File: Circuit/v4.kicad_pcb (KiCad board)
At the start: 2 copper layers, 30 x 50 mm, 43 parts, among them J2 AVR-ISP-6, Q1 IRLML6244TRPBF, U1 HMHA2801, U4 ATtiny841-SSU

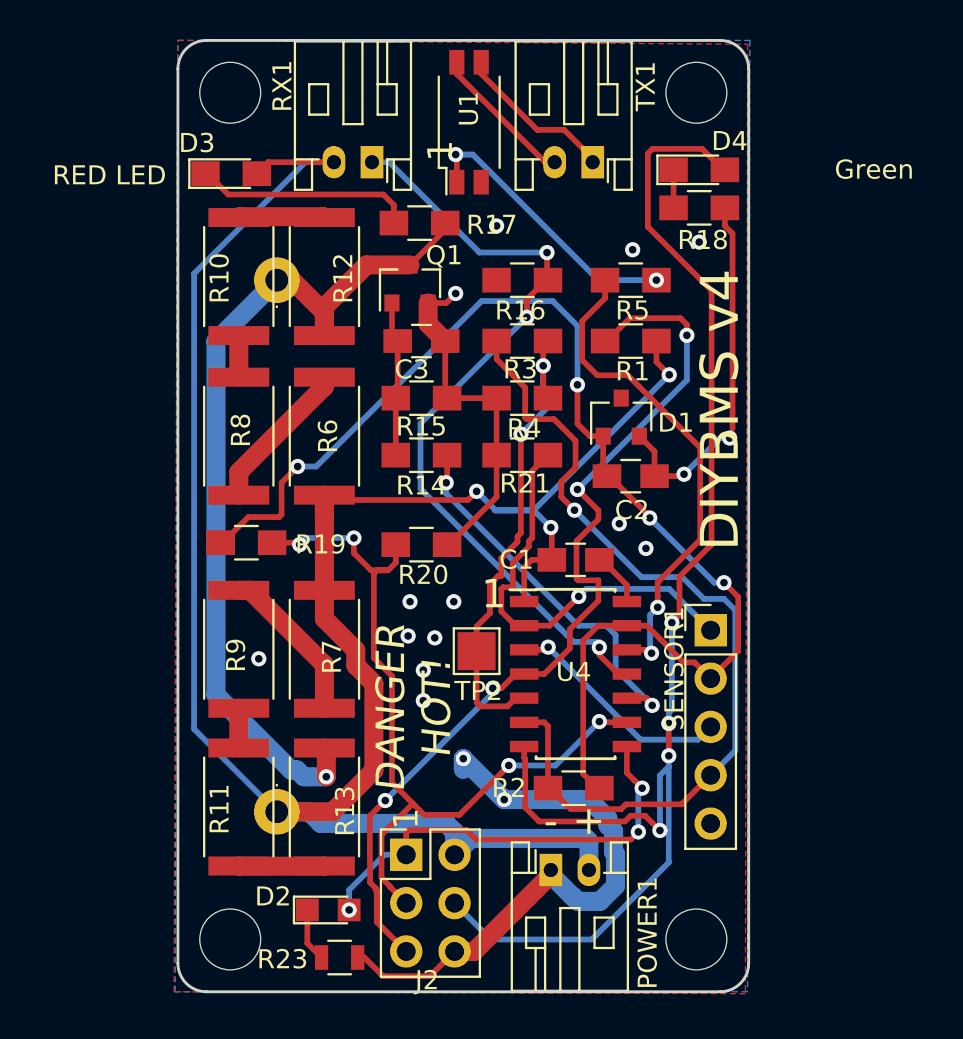
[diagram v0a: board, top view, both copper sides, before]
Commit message: add jlcpcb_assembly branch
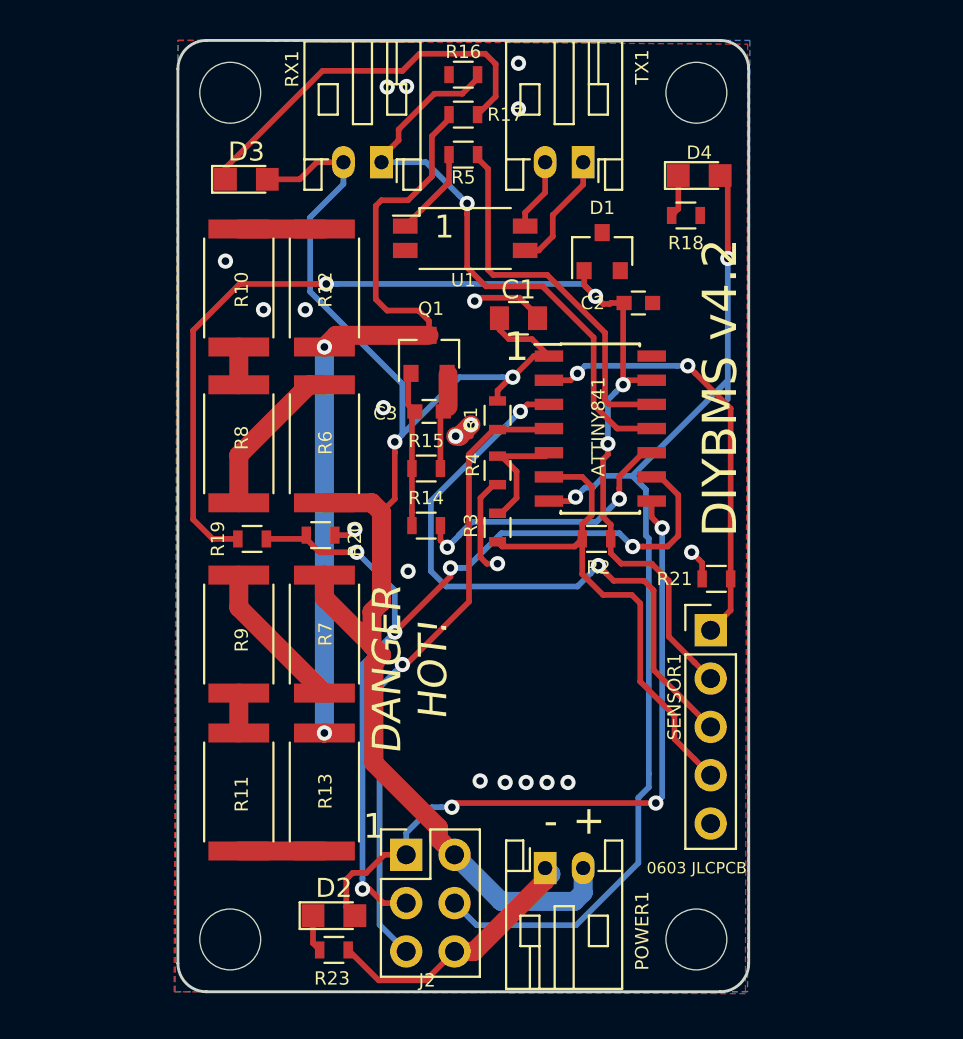
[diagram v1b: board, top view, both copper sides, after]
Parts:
- removed R22: 4R4, Resistors_THT:R_Axial_Power_L25.0mm_W9.0mm_P27.94mm
- removed TP2: TestPoint, TestPoint:TestPoint_Pad_2.0x2.0mm
- removed U4: ATtiny841-SSU, Housings_SOIC:SOIC-14_3.9x8.7mm_Pitch1.27mm
- added ATTINY841: ATtiny841-SSU, Housings_SOIC:SOIC-14_3.9x8.7mm_Pitch1.27mm, F.Cu at (124.1, 68.4)
- C1: footprint Capacitors_SMD:C_0805_HandSoldering -> Capacitors_SMD:C_0805
- C2: footprint Capacitors_SMD:C_0805_HandSoldering -> Capacitors_SMD:C_0603
- C3: value 10uF 10V -> MLCC 10UF 10V; footprint Capacitors_SMD:C_0805_HandSoldering -> Capacitors_SMD:C_0603
- D1: value LM4040BIM3-2.0/NOPB, 2.048V, SOT-23-3 -> ADR5040BRTZ-REEL7 2.048V
- D3: value RED LED -> Red; footprint LEDs:LED_0805_HandSoldering -> LEDs:LED_0805
- D4: footprint LEDs:LED_0805_HandSoldering -> LEDs:LED_0805
- R1, R14, R15, R16, R17, R18, R2, R20, R21, R5: footprint Resistors_SMD:R_0805_HandSoldering -> Resistors_SMD:R_0603
- R10, R11, R12, R13, R6, R7, R8, R9: value 2R2 1W -> 2R 1W
- R19: value SDNT2012X473F4150FTF -> NCP18WB473J03RB; footprint Resistors_SMD:R_0805_HandSoldering -> Resistors_SMD:R_0603
- R23: value 2K2 -> 1K8; footprint Resistors_SMD:R_0805 -> Resistors_SMD:R_0603
- R3: value 475K E96 series (tolerance 1%) -> 470KOHMS ±1% 1/10W; footprint Resistors_SMD:R_0805_HandSoldering -> Resistors_SMD:R_0603
- R4: value 402K E96 series (tolerance 1%) -> 390KOHMS ±1% 1/10W; footprint Resistors_SMD:R_0805_HandSoldering -> Resistors_SMD:R_0603
- U1: value HMHA2801 -> EL3H7(B)(TA)-G
- moved R2 13.2 mm to (123.9, 74.2)
- moved C1 13.0 mm to (119.8, 62.6)
- moved R21 12.1 mm to (130.2, 76.3)
- moved R16 11.2 mm to (116.9, 49.8)
- moved R5 11.0 mm to (116.9, 54.0), turned to 0 degrees
- moved R3 9.89 mm to (118.7, 73.6), turned to 90 degrees
- moved C2 9.11 mm to (126.1, 61.8)
- moved D1 8.76 mm to (124.2, 59.1)
- moved R1 8.01 mm to (118.7, 67.7), turned to 270 degrees
- moved R17 6.15 mm to (116.9, 51.9), turned to 0 degrees
- moved U1 6.10 mm to (117.0, 58.4), turned to 0 degrees
- moved R20 5.32 mm to (109.4, 74.0)
- moved R4 4.02 mm to (118.7, 70.6), turned to 270 degrees
- moved Q1 3.83 mm to (115.1, 64.5)
- moved C3 3.72 mm to (115.1, 67.5)
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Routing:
- net VCC: track 118.8 -> 80.1 mm, vias 3 -> 2
- net GND: track 71.1 -> 33.4 mm, vias 17 -> 20
- net Net-(ATTINY841-Pad3): track 12.2 -> 33.4 mm, vias 1 -> 2
- net ENABLE: track 46.2 -> 26.2 mm, vias 1 -> 0
- net Net-(ATTINY841-Pad5): track 25.4 -> 6.84 mm, vias 2 -> 0
- net Net-(ATTINY841-Pad7): track 72.5 -> 56.6 mm, vias 4 -> 2
- net Net-(ATTINY841-Pad4): track 49.2 -> 33.5 mm, vias 4 -> 1
- net Net-(ATTINY841-Pad8): track 23.5 -> 36.9 mm
- net RXD0: track 41.7 -> 31.6 mm, vias 3 -> 1
- net Net-(R5-Pad1): track 14.8 -> 4.71 mm, vias 2 -> 0
- net Net-(D3-Pad1): track 11.5 -> 20.6 mm
- net Net-(ATTINY841-Pad9): track 42.6 -> 48.9 mm, vias 4 -> 5
- net TXD0: track 26.1 -> 19.9 mm, vias 2 -> 0
- net DUMP_LOAD_ENABLE: track 20.1 -> 14.8 mm
- net Net-(Q1-Pad3): track 46.6 -> 42.2 mm, vias 1 -> 2
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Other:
- board text added: "0603 JLCPCB"
- board text added: "1 Jan 2020"
- board text added: "DIYBMS v4.2"
- board text added: "©2019/2020 Stuart Pittaway"
- board text removed: "23 June 2019"
- board text removed: "DIYBMS v4"
- board text removed: "©2019 Stuart Pittaway"

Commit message: Updated BOM and CPL files
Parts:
- C3: value MLCC 10UF 10V -> 10uF X5R
- Q1: value IRLML6244TRPBF -> AO3400A
- R1: value 10K -> 10KOHMS
- R10, R11, R12, R13, R6, R7, R8, R9: value 2R 1W -> 2OHMS
- R14, R5: value 510R -> 510OHMS
- R15, R20, R21: value 47K -> 47KOHMS
- R16: value 4K7 -> 4.7KOHMS
- R17, R18: value 2K2 -> 2.2KOHMS
- R2: value 1K -> 1KOHMS
- R23: value 1K8 -> 1.8KOHMS
- R3: value 470KOHMS ±1% 1/10W -> 470KOHMS
- R4: value 390KOHMS ±1% 1/10W -> 390KOHMS
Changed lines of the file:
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@@
   (page A4)
   (layers
-    (0 F.Cu signal hide)
-    (31 B.Cu signal hide)
+    (0 F.Cu signal)
+    (31 B.Cu signal)
     (32 B.Adhes user)
     (33 F.Adhes user hide)
@@
       (effects (font (size 0.7 0.7) (thickness 0.1)))
     )
-    (fp_text value 1K8 (at -1.3 -1 180) (layer F.Fab) hide
+    (fp_text value 1.8KOHMS (at -1.3 -1 180) (layer F.Fab) hide
       (effects (font (size 0.7 0.7) (thickness 0.1)))
     )
@@
       (effects (font (size 0.7 0.7) (thickness 0.1)))
     )
-    (fp_text value 47K (at -0.5 1.2 180) (layer F.Fab)
+    (fp_text value 47KOHMS (at -0.5 1.2 180) (layer F.Fab)
       (effects (font (size 0.7 0.7) (thickness 0.1)))
     )
@@
       (effects (font (size 0.7 0.7) (thickness 0.1)))
     )
-    (fp_text value 47K (at 0 1.5) (layer F.Fab)
+    (fp_text value 47KOHMS (at 0 1.5) (layer F.Fab)
       (effects (font (size 0.7 0.7) (thickness 0.1)))
     )
@@
       (effects (font (size 0.7 0.7) (thickness 0.1)))
     )
-    (fp_text value 2K2 (at -0.8 -2.7 180) (layer F.Fab)
+    (fp_text value 2.2KOHMS (at -0.8 -2.7 180) (layer F.Fab)
       (effects (font (size 0.7 0.7) (thickness 0.1)))
     )
@@
       (effects (font (size 0.7 0.7) (thickness 0.1)))
     )
-    (fp_text value 2K2 (at 0 -0.1) (layer F.Fab)
+    (fp_text value 2.2KOHMS (at 0 -0.1) (layer F.Fab)
       (effects (font (size 0.7 0.7) (thickness 0.1)))
     )
@@
       (effects (font (size 0.7 0.7) (thickness 0.1)))
     )
-    (fp_text value 4K7 (at -2.3 0) (layer F.Fab)
+    (fp_text value 4.7KOHMS (at -2.3 0) (layer F.Fab)
       (effects (font (size 0.7 0.7) (thickness 0.1)))
     )
@@
       (effects (font (size 0.7 0.7) (thickness 0.1)))
     )
-    (fp_text value 47K (at 0 1.5) (layer F.Fab)
+    (fp_text value 47KOHMS (at 0 1.5) (layer F.Fab)
       (effects (font (size 0.7 0.7) (thickness 0.1)))
     )
@@
       (effects (font (size 0.7 0.7) (thickness 0.1)))
     )
-    (fp_text value 510R (at 0 1.5) (layer F.Fab)
+    (fp_text value 510OHMS (at 0 1.5) (layer F.Fab)
       (effects (font (size 0.7 0.7) (thickness 0.1)))
     )
@@
       (effects (font (size 0.7 0.7) (thickness 0.1)))
     )
-    (fp_text value 510R (at 2.7 0.2) (layer F.Fab)
+    (fp_text value 510OHMS (at 2.7 0.2) (layer F.Fab)
       (effects (font (size 0.7 0.7) (thickness 0.1)))
     )
@@
       (effects (font (size 0.7 0.7) (thickness 0.1)))
     )
-    (fp_text value "390KOHMS ±1% 1/10W" (at 0 1.5 270) (layer F.Fab)
+    (fp_text value 390KOHMS (at 0 1.5 270) (layer F.Fab)
       (effects (font (size 0.7 0.7) (thickness 0.1)))
     )
@@
       (effects (font (size 0.7 0.7) (thickness 0.1)))
     )
-    (fp_text value "470KOHMS ±1% 1/10W" (at 0 1.5 90) (layer F.Fab) hide
+    (fp_text value 470KOHMS (at 0 1.5 90) (layer F.Fab) hide
       (effects (font (size 0.7 0.7) (thickness 0.1)))
     )
@@
       (effects (font (size 0.7 0.7) (thickness 0.1)))
     )
-    (fp_text value 1K (at 0 1.5) (layer F.Fab)
+    (fp_text value 1KOHMS (at 0 1.5) (layer F.Fab)
       (effects (font (size 0.7 0.7) (thickness 0.1)))
     )
@@
       (effects (font (size 0.7 0.7) (thickness 0.1)))
     )
-    (fp_text value 10K (at 0 1.5 270) (layer F.Fab)
+    (fp_text value 10KOHMS (at 0.1 -1.2 270) (layer F.Fab)
       (effects (font (size 0.7 0.7) (thickness 0.1)))
     )
@@
       (effects (font (size 0.7 0.7) (thickness 0.1)))
     )
-    (fp_text value "MLCC 10UF 10V" (at 0 1.5) (layer F.Fab)
+    (fp_text value "10uF X5R" (at 0 1.5) (layer F.Fab)
       (effects (font (size 0.7 0.7) (thickness 0.1)))
     )
@@
       (effects (font (size 0.7 0.7) (thickness 0.1)))
     )
-    (fp_text value IRLML6244TRPBF (at 0.05 -21.7 180) (layer F.Fab)
+    (fp_text value AO3400A (at 2.4 -1.2 180) (layer F.Fab)
       (effects (font (size 0.7 0.7) (thickness 0.1)))
     )
@@
       (effects (font (size 0.7 0.7) (thickness 0.1)))
     )
-    (fp_text value "2R 1W" (at 0.1288 0.0508 90) (layer F.Fab)
+    (fp_text value 2OHMS (at 0.1288 0.0508 90) (layer F.Fab)
       (effects (font (size 0.7 0.7) (thickness 0.1)))
     )
@@
       (effects (font (size 0.7 0.7) (thickness 0.1)))
     )
-    (fp_text value "2R 1W" (at 0.0272 0 270) (layer F.Fab)
+    (fp_text value 2OHMS (at 0.0272 0 270) (layer F.Fab)
       (effects (font (size 0.7 0.7) (thickness 0.1)))
     )
@@
       (effects (font (size 0.7 0.7) (thickness 0.1)))
     )
-    (fp_text value "2R 1W" (at -0.2404 -0.016934 90) (layer F.Fab)
+    (fp_text value 2OHMS (at -0.2404 -0.016934 90) (layer F.Fab)
       (effects (font (size 0.7 0.7) (thickness 0.1)))
     )
@@
       (effects (font (size 0.7 0.7) (thickness 0.1)))
     )
-    (fp_text value "2R 1W" (at -0.088 0.084666 270) (layer F.Fab)
+    (fp_text value 2OHMS (at -0.088 0.084666 270) (layer F.Fab)
       (effects (font (size 0.7 0.7) (thickness 0.1)))
     )
@@
       (effects (font (size 0.7 0.7) (thickness 0.1)))
     )
-    (fp_text value "2R 1W" (at 0.1796 0.084667 90) (layer F.Fab)
+    (fp_text value 2OHMS (at 0.1796 0.084667 90) (layer F.Fab)
       (effects (font (size 0.7 0.7) (thickness 0.1)))
     )
@@
       (effects (font (size 0.7 0.7) (thickness 0.1)))
     )
-    (fp_text value "2R 1W" (at -0.176 0.135468 270) (layer F.Fab)
+    (fp_text value 2OHMS (at -0.176 0.135468 270) (layer F.Fab)
       (effects (font (size 0.7 0.7) (thickness 0.1)))
     )
@@
       (effects (font (size 0.7 0.7) (thickness 0.1)))
     )
-    (fp_text value "2R 1W" (at -0.1388 0.1016 270) (layer F.Fab)
+    (fp_text value 2OHMS (at -0.1388 0.1016 270) (layer F.Fab)
       (effects (font (size 0.7 0.7) (thickness 0.1)))
     )
@@
       (effects (font (size 0.7 0.7) (thickness 0.1)))
     )
-    (fp_text value "2R 1W" (at 0 0.0508 90) (layer F.Fab)
+    (fp_text value 2OHMS (at 0 0.0508 90) (layer F.Fab)
       (effects (font (size 0.7 0.7) (thickness 0.1)))
     )
@@
   (segment (start 116.4576 95.8676) (end 114.9376 97.3876) (width 0.3) (layer F.Cu) (net 1))
   (segment (start 114.9376 97.3876) (end 112.4676 97.3876) (width 0.3) (layer F.Cu) (net 1))
-  (via (at 119.1176 86.9876) (size 0.8) (drill 0.4) (layers F.Cu B.Cu) (net 1))
-  (via (at 120.2176 86.9876) (size 0.8) (drill 0.4) (layers F.Cu B.Cu) (net 1))
-  (via (at 121.3176 86.9876) (size 0.8) (drill 0.4) (layers F.Cu B.Cu) (net 1))
-  (via (at 122.4176 86.9876) (size 0.8) (drill 0.4) (layers F.Cu B.Cu) (net 1))
+  (via (at 117.7176 86.9876) (size 0.8) (drill 0.4) (layers F.Cu B.Cu) (net 1))
+  (via (at 120.1176 86.9876) (size 0.8) (drill 0.4) (layers F.Cu B.Cu) (net 1))
+  (via (at 122.5176 86.9876) (size 0.8) (drill 0.4) (layers F.Cu B.Cu) (net 1))
+  (via (at 124.9176 86.9876) (size 0.8) (drill 0.4) (layers F.Cu B.Cu) (net 1))
   (via (at 117.3176 68.1876) (size 0.8) (drill 0.4) (layers F.Cu B.Cu) (net 1))
   (via (at 106.4176 62.13761) (size 0.8) (drill 0.4) (layers F.Cu B.Cu) (net 1))
@@
   (segment (start 117.817599 75.153284) (end 118.151915 75.4876) (width 0.3) (layer F.Cu) (net 1))
   (via (at 114.0176 75.8876) (size 0.8) (drill 0.4) (layers F.Cu B.Cu) (net 1))
-  (via (at 117.80187 86.908949) (size 0.8) (drill 0.4) (layers F.Cu B.Cu) (net 1))
+  (via (at 115.3176 86.9876) (size 0.8) (drill 0.4) (layers F.Cu B.Cu) (net 1))
   (segment (start 110.9176 73.9876) (end 111.219064 73.686136) (width 0.3) (layer F.Cu) (net 1))
   (segment (start 110.1676 73.9876) (end 110.9176 73.9876) (width 0.3) (layer F.Cu) (net 1))

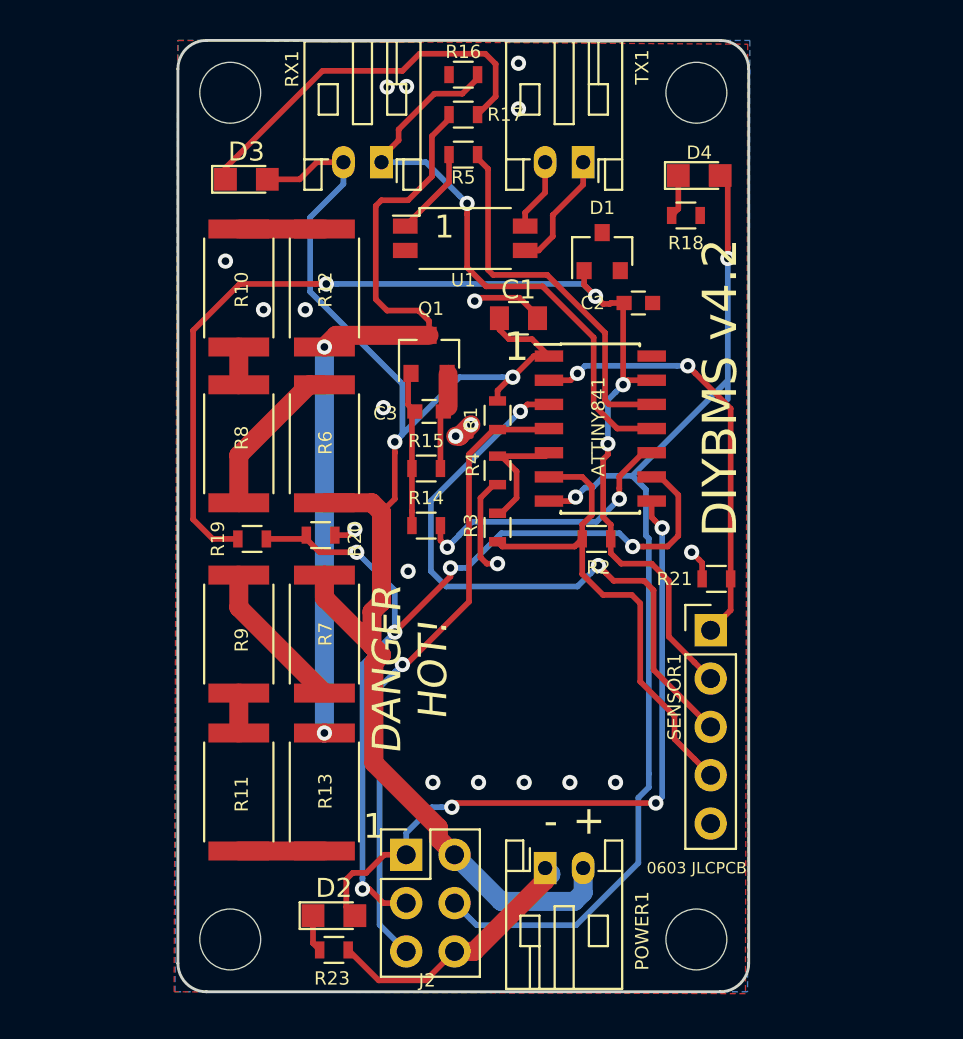
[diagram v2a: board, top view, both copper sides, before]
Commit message: Resistor array using 1206 parts
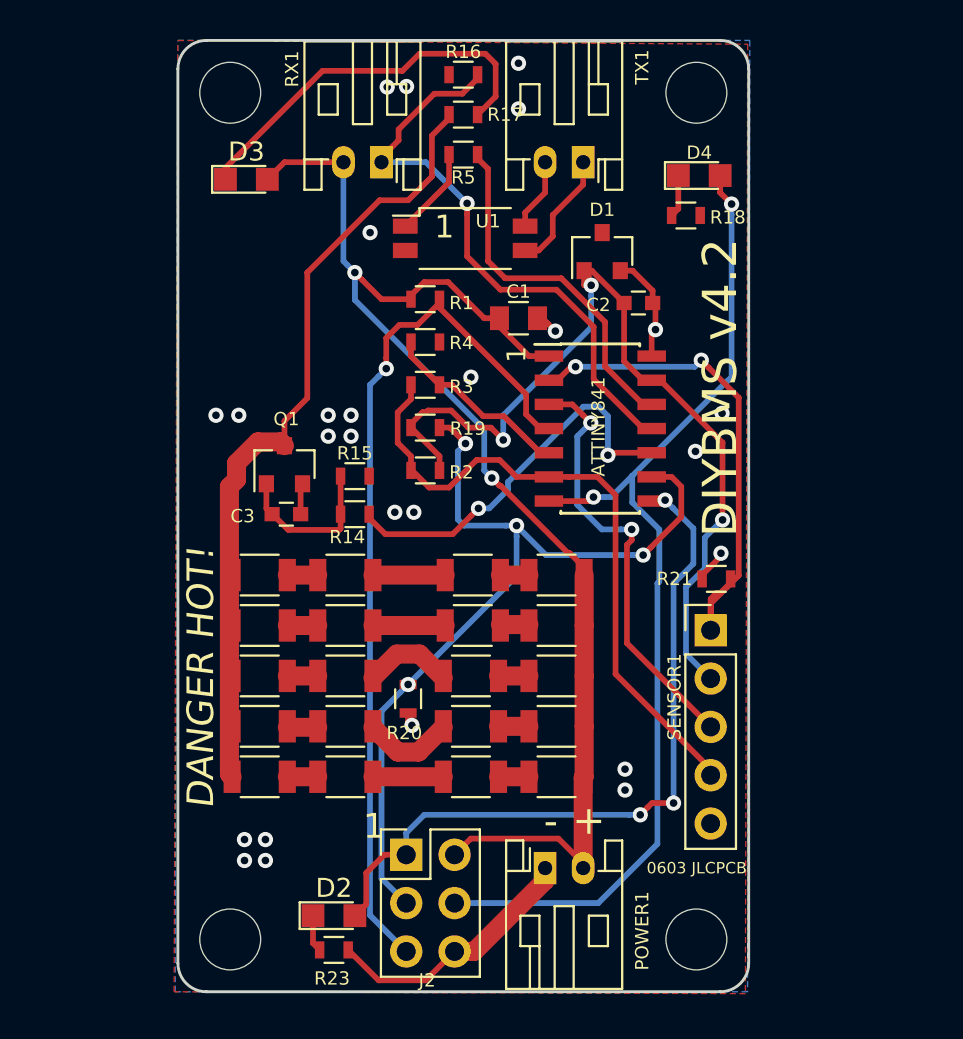
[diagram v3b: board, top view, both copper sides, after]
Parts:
- added R22: 6.2OHMS, Resistors_SMD:R_1206, F.Cu at (121.8, 86.7)
- added R24: 6.2OHMS, Resistors_SMD:R_1206, F.Cu at (121.8, 84.0)
- added R25: 6.2OHMS, Resistors_SMD:R_1206, F.Cu at (117.3, 86.7)
- added R26: 6.2OHMS, Resistors_SMD:R_1206, F.Cu at (117.3, 84.0)
- added R27: 6.2OHMS, Resistors_SMD:R_1206, F.Cu at (110.7, 86.7)
- added R28: 6.2OHMS, Resistors_SMD:R_1206, F.Cu at (110.7, 84.0)
- added R29: 6.2OHMS, Resistors_SMD:R_1206, F.Cu at (106.2, 86.7)
- added R30: 6.2OHMS, Resistors_SMD:R_1206, F.Cu at (106.2, 84.0)
- added R31: 6.2OHMS, Resistors_SMD:R_1206, F.Cu at (121.8, 76.1)
- added R32: 6.2OHMS, Resistors_SMD:R_1206, F.Cu at (117.4, 76.1)
- added R33: 6.2OHMS, Resistors_SMD:R_1206, F.Cu at (110.7, 76.1)
- added R34: 6.2OHMS, Resistors_SMD:R_1206, F.Cu at (106.2, 76.1)
- R10, R11, R12, R13, R6, R7, R8, R9: value 2OHMS -> 6.2OHMS; footprint Resistors_SMD:R_2512 -> Resistors_SMD:R_1206
- moved R10 21.1 mm to (110.7, 81.4), turned to 180 degrees
- moved R12 20.7 mm to (106.2, 81.4), turned to 180 degrees
- moved R6 17.3 mm to (121.8, 81.4), turned to 180 degrees
- moved R8 17.3 mm to (117.3, 81.4), turned to 180 degrees
- moved R9 12.3 mm to (117.4, 78.7), turned to 180 degrees
- moved R7 12.2 mm to (121.8, 78.7), turned to 180 degrees
- moved R19 10.8 mm to (114.9, 68.3)
- moved R11 10.4 mm to (110.7, 78.7), turned to 180 degrees
- moved R20 9.75 mm to (114.0, 82.6), turned to 270 degrees
- moved R2 9.69 mm to (114.9, 70.6)
- moved Q1 9.56 mm to (107.5, 70.3)
- moved R13 9.39 mm to (106.2, 78.7), turned to 180 degrees
- moved C3 9.24 mm to (107.6, 72.9)
- moved R3 8.41 mm to (114.9, 66.1), turned to 0 degrees
- moved R4 7.75 mm to (114.9, 63.8), turned to 0 degrees
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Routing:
- net 2_VOLT: track 63.5 -> 46.6 mm, vias 4 -> 3
- net Net-(ATTINY841-Pad4): track 33.5 -> 46.6 mm
- net VCC: track 80.1 -> 67.9 mm
- net Net-(ATTINY841-Pad3): track 33.4 -> 22.9 mm
- net GND: track 33.4 -> 25.2 mm, vias 20 -> 26
- net ENABLE: track 26.2 -> 34.4 mm
- net Net-(R6-Pad2): track 8.53 -> 1.60 mm
- net Net-(R7-Pad2): track 8.06 -> 1.50 mm
- net DUMP_LOAD_ENABLE: track 14.8 -> 20.7 mm
- net Net-(R26-Pad2): track 0.00 -> 4.78 mm
- net Net-(ATTINY841-Pad2): track 22.9 -> 27.3 mm
- net Net-(R32-Pad2): track 0.00 -> 3.80 mm
- net Net-(R25-Pad2): track 0.00 -> 3.70 mm
- net Net-(ATTINY841-Pad5): track 6.84 -> 10.1 mm
- net Net-(ATTINY841-Pad9): track 48.9 -> 45.9 mm, vias 5 -> 4
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
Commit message: Order submitted to JLCPCB
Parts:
- removed C2: 2.2uF, Capacitors_SMD:C_0603
- D1: value ADR5040BRTZ-REEL7 2.048V -> AZ432ANTR-E1
- R3: value 470KOHMS -> 68KOHMS
- R4: value 390KOHMS -> 27KOHMS
- moved D1 0.58 mm to (124.7, 58.8)
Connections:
- D1 pad 2: GND -> 2_VOLT
- D1 pad 3: (no net) -> GND
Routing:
- net 2_VOLT: track 46.6 -> 50.8 mm, vias 3 -> 6
- net GND: track 25.2 -> 20.9 mm
- net ENABLE: track 34.4 -> 35.9 mm
- net VCC: track 67.9 -> 69.2 mm
- net Net-(ATTINY841-Pad7): track 55.1 -> 56.1 mm
- net Net-(ATTINY841-Pad5): track 10.1 -> 11.0 mm
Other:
- board text added: "6 Jan 2020"
- board text added: "DO NOT SHORT CIRCUIT DO NOT REVERSE POLARITY MAX 4.4V BATTERY INPUT 850mA DUMP LOAD"
- board text removed: "1 Jan 2020"
- board text removed: "DO NOT SHORT CIRCUIT DO NOT REVERSE POLARITY MAX 4.5V BATTERY INPUT 1 AMP DUMP LOAD"
